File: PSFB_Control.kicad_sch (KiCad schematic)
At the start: 17 parts, among them J2 PSFB_Control_1, U6 USBLC6-2SC6, U7 USBLC6-2SC6

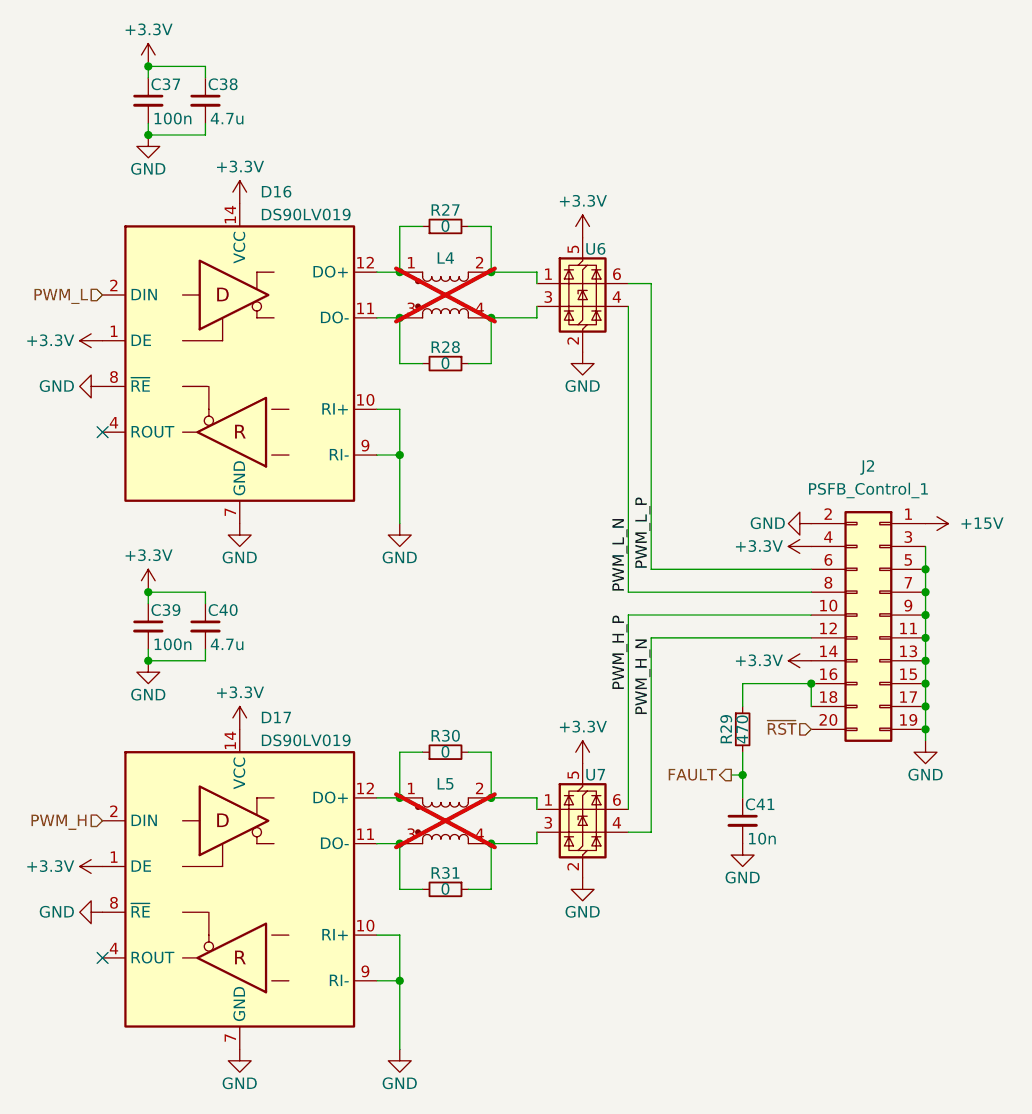
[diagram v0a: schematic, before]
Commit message: VER1.0: добавил схему с измерением напряжения и заменил LVDS трансиверы
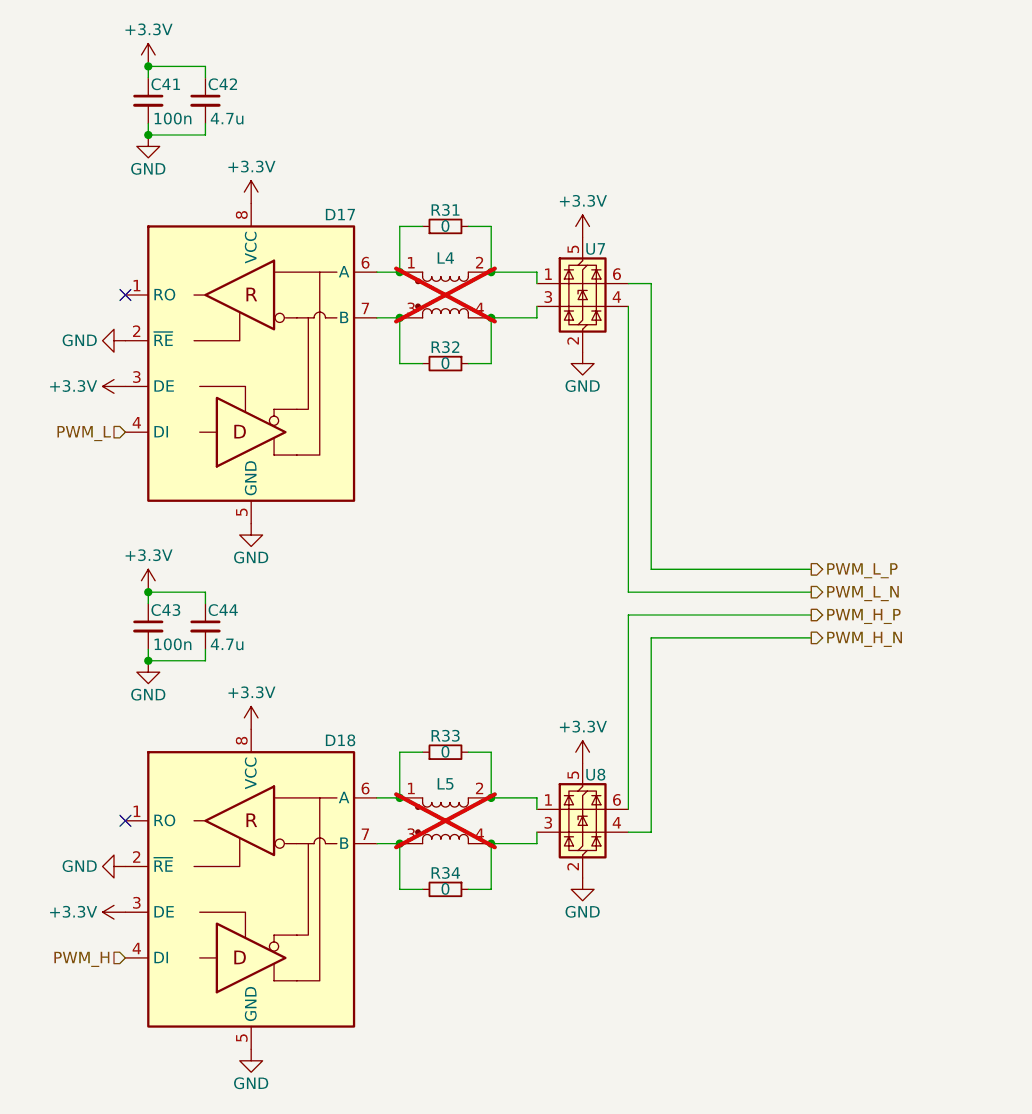
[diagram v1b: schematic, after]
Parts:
- removed C41: 10n, Capacitor_SMD:C_0805_2012Metric_Pad1.18x1.45mm_HandSolder, symbol Device:C_Small
- removed D16, D17: DS90LV019, Package_SO:SO-14_3.9x8.65mm_P1.27mm, symbol Interface_my:DS90L019TMx
- removed J2: PSFB_Control_1, Connector_IDC:IDC-Header_2x10_P2.54mm_Vertical, symbol Connector_Generic:Conn_02x10_Odd_Even
- removed R29: 470, Resistor_SMD:R_0805_2012Metric_Pad1.20x1.40mm_HandSolder, symbol Device:R_Small
- added D17, D18: (no value), Package_SO:SO-8_3.9x4.9mm_P1.27mm, symbol Interface_my:MS2111
- renumbered C37 to C41, C38 to C42, C39 to C43, C40 to C44, R27 to R31, R28 to R32, R30 to R33, R31 to R34, U6 to U7, U7 to U8
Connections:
- net +3.3V: now also D17.3 (DE), D17.8 (VCC), D18.3 (DE), D18.8 (VCC)
- net GND: now also D17.2 (~{RE}), D17.5 (GND), D18.2 (~{RE}), D18.5 (GND)
- net PWM_H: now also D18.4 (DI)
- net PWM_L: now also D17.4 (DI)
- net at L4.3, R32.2: now also D17.7 (B)
- net at L5.3, R34.2: now also D18.7 (B)
- net at L5.1, R33.1: now also D18.6 (NC)
- net at L4.1, R31.1: now also D17.6 (NC)

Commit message: VER1.0: добавил разделение питания VDD и VDDA
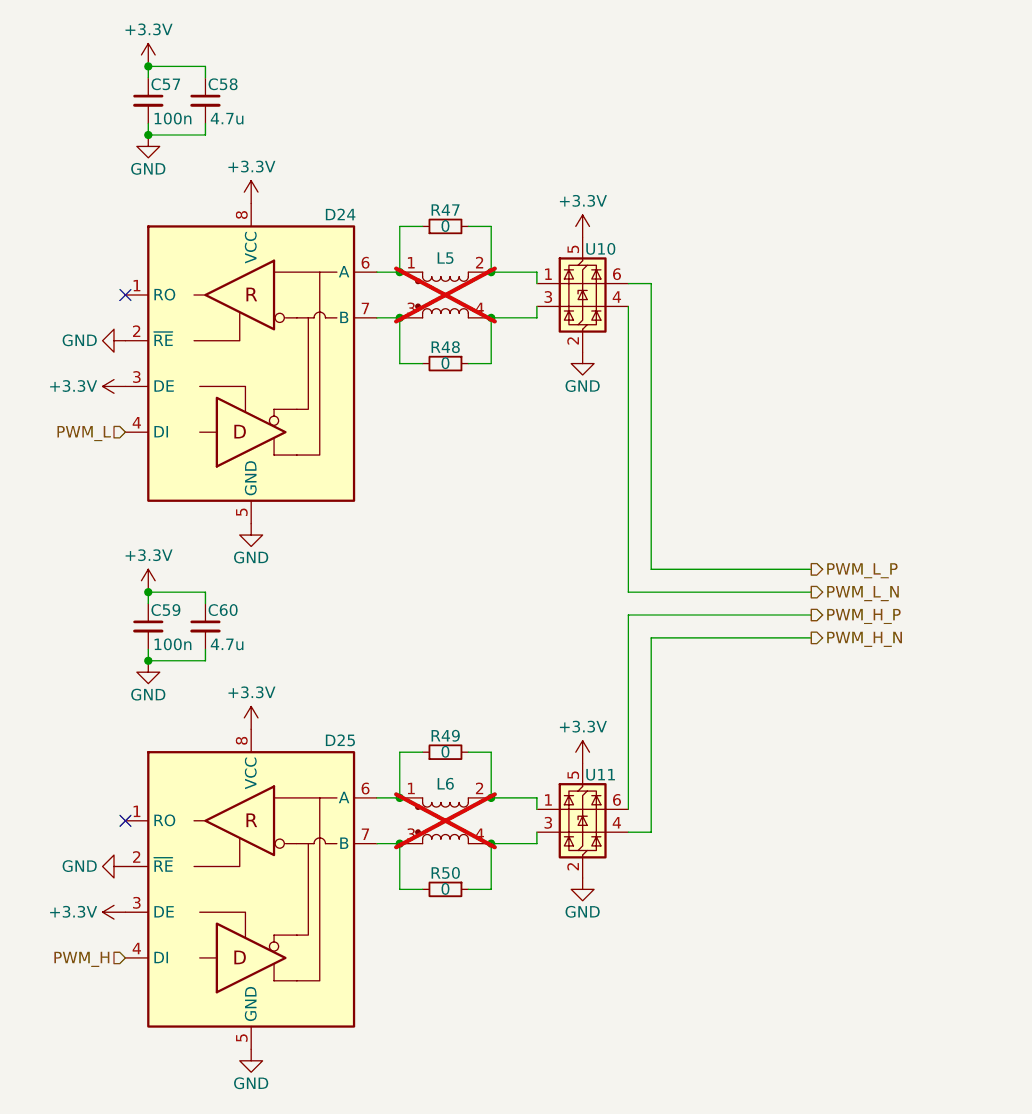
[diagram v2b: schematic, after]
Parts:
- C57: renamed from C41; Description P/N (none) -> Capacitor SMD 25V
- C58: renamed from C42; Description P/N (none) -> Capacitor SMD 25V
- C59: renamed from C43; Description P/N (none) -> Capacitor SMD 25V
- C60: renamed from C44; Description P/N (none) -> Capacitor SMD 25V
- L5: renamed from L4; value DLW21SN900SQ2L -> (none); Description P/N (none) -> Inductor SMD; Product Name (none) -> DLW21SN900SQ2L
- L6: renamed from L5; value DLW21SN900SQ2L -> (none); Description P/N (none) -> Inductor SMD; Product Name (none) -> DLW21SN900SQ2L
- R47: renamed from R31; Description P/N (none) -> Resistor SMD 1%
- R48: renamed from R32; Description P/N (none) -> Resistor SMD 1%
- R49: renamed from R33; Description P/N (none) -> Resistor SMD 1%
- R50: renamed from R34; Description P/N (none) -> Resistor SMD 1%
- U10: renamed from U7; value USBLC6-2SC6 -> (none); Description P/N (none) -> ESD protection; Product Name (none) -> USBLC6-2SC6
- U11: renamed from U8; value USBLC6-2SC6 -> (none); Description P/N (none) -> ESD protection; Product Name (none) -> USBLC6-2SC6
- renumbered D17 to D24, D18 to D25
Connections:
- net at D24.6 (NC): now also L5.1, R47.1

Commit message: VER1.0: раскидал компоненты на плате
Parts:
- removed L5, L6: (no value), Inductor_SMD:L_CommonModeChoke_Coilcraft_0805USB, symbol Device:L_Coupled
- removed R47, R48, R49, R50: 0, Resistor_SMD:R_0805_2012Metric_Pad1.20x1.40mm_HandSolder, symbol Device:R_Small
- removed U10, U11: (no value), Package_TO_SOT_SMD:SOT-23-6, symbol Power_Protection:USBLC6-2SC6
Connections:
- net PWM_H_N: now also D25.7 (B)
- net PWM_H_P: now also D25.6 (NC)
- net PWM_L_N: now also D24.7 (B)
- net PWM_L_P: now also D24.6 (NC)
